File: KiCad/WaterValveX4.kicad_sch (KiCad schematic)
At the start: 51 parts, among them J1 Conn_01x04_Male, J2 Barrel_Jack, J3 Conn_01x03_Male, J4 Conn_01x01_Male, J5 Conn_01x04_Male, J6 Screw_Terminal_01x03, J7 Screw_Terminal_01x03, J8 Screw_Terminal_01x03, J9 Screw_Terminal_01x02, Q1 IRLML2502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

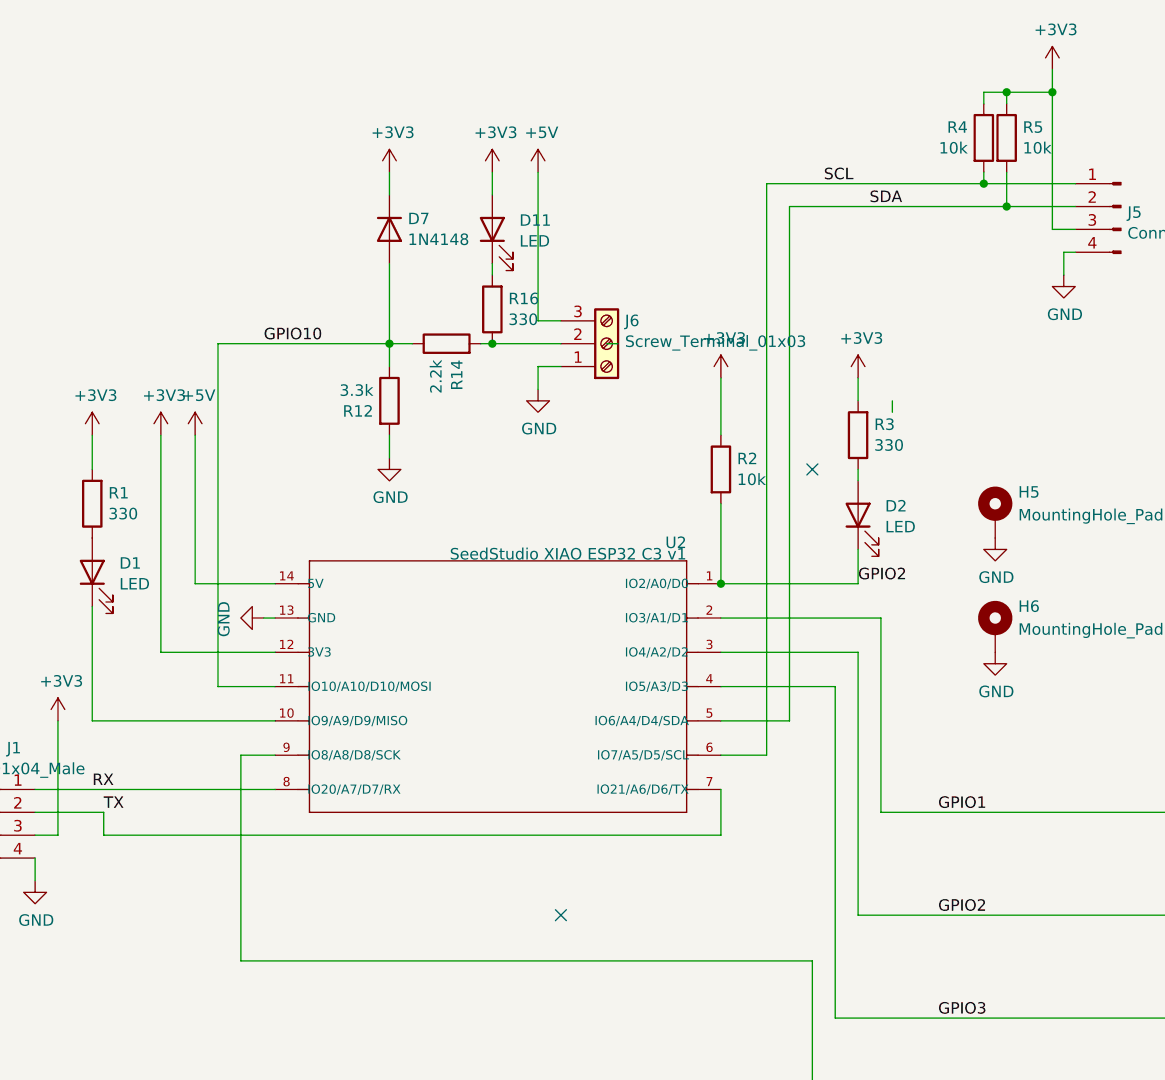
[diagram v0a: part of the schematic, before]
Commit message: Version 2.0.1 - pulled up / level shifted flow input
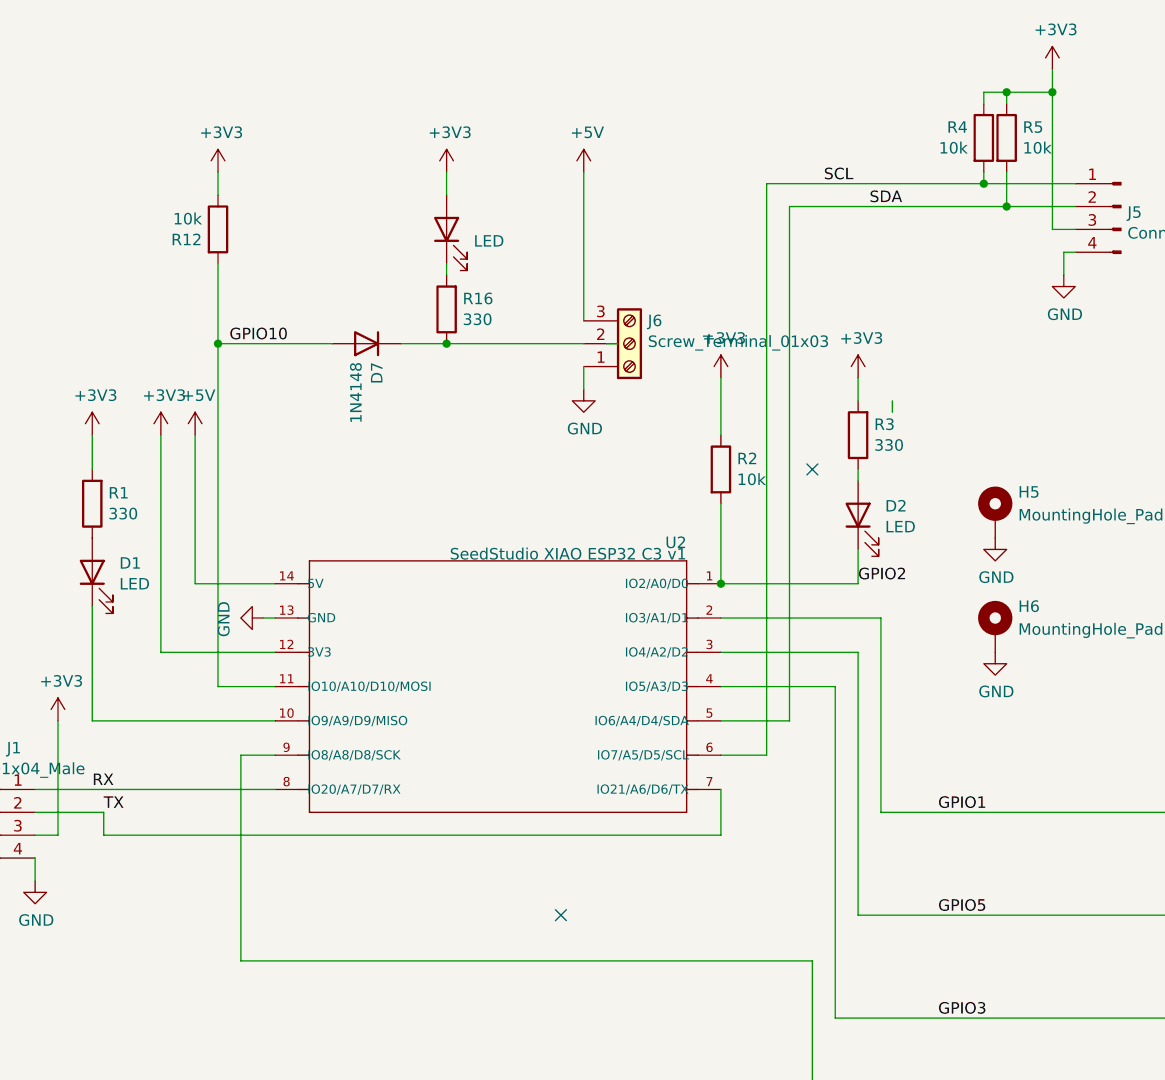
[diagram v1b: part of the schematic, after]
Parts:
- removed R14: 2.2k, Resistor_SMD:R_0805_2012Metric_Pad1.20x1.40mm_HandSolder, symbol Device:R
- R12: value 3.3k -> 10k
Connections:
- net +3V3: now also R12.1; no longer D7.1 (K)
- net GND: no longer R12.2
- net GPIO10: now also R12.2; no longer R12.1
- net GPIO2: no longer R8.1, U2.3 (IO4/A2/D2)
- net at J6.2 (Pin_2), R16.1: now also D7.1 (K)
- new net GPIO5: R8.1, U2.3 (IO4/A2/D2)
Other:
- moved on the sheet: J6, R16

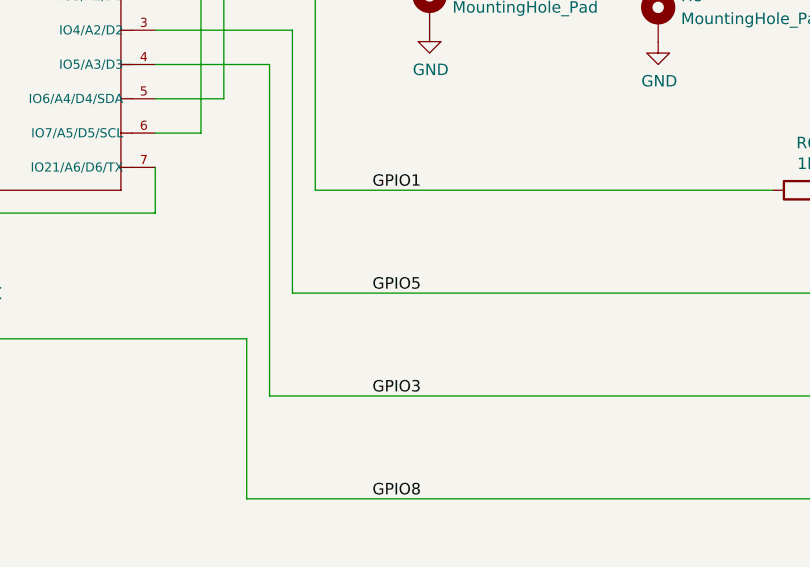
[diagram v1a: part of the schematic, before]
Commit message: Fixed KiCAD GPIO labels
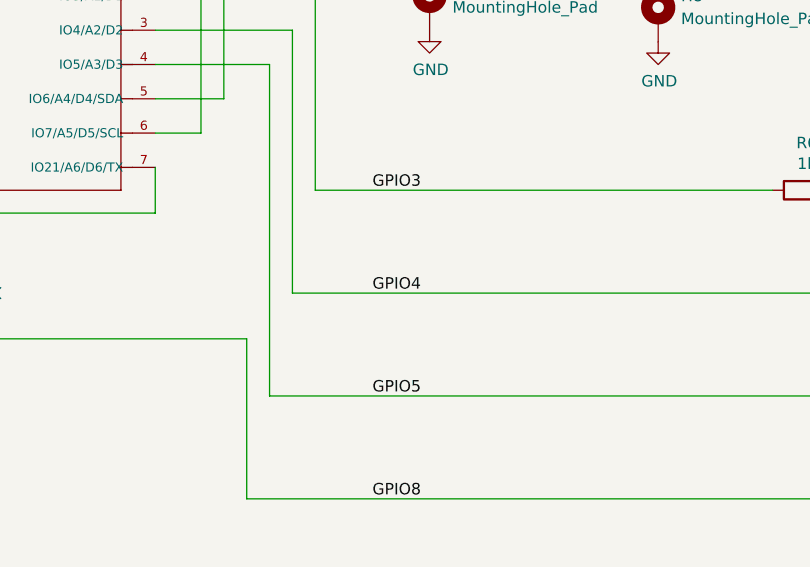
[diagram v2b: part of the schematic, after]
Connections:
- net GPIO1 is gone; now on net GPIO3: R6.1, U2.2 (IO3/A1/D1)
- net GPIO3: no longer R9.1, U2.4 (IO5/A3/D3)
- net GPIO5: now also R9.1, U2.4 (IO5/A3/D3); no longer R8.1, U2.3 (IO4/A2/D2)
- new net GPIO4: R8.1, U2.3 (IO4/A2/D2)
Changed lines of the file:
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@@
 		)
 	)
-	(label "GPIO5"
+	(label "GPIO4"
 		(at 125.73 115.57 0)
 		(fields_autoplaced yes)
@@
 		)
 	)
-	(label "GPIO3"
+	(label "GPIO5"
 		(at 125.73 127 0)
 		(fields_autoplaced yes)
@@
 		)
 	)
-	(label "GPIO1"
+	(label "GPIO3"
 		(at 125.73 104.14 0)
 		(fields_autoplaced yes)

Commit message: Change to use ESP32 C6 THT
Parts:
- removed U2: SeedStudio XIAO ESP32 C3 v1, LOCAL1:XIAO_ESP32C3_THT, symbol LOCAL1:XIAO_ESP32C3_THT
- added U2: XIAO-ESP32-C6, LOCAL1:XIAO-ESP32-C6-DIP, symbol LOCAL1:XIAO_ESP32-C6-DIP
- D11: footprint LED_SMD:LED_0805_2012Metric_Pad1.15x1.40mm_HandSolder -> LED_THT:LED_D5.0mm
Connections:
- net +3V3: now also U2.12 (3V3)
- net +5V: now also U2.14 (VBUS)
- net GND: now also U2.13 (GND)
- net GPIO10: now also U2.11 (GPIO18/D10/MOSI)
- net GPIO2: now also U2.1 (GPIO0/A0/D0)
- net GPIO3: now also U2.2 (GPIO1/A1/D1)
- net GPIO4: now also U2.3 (GPIO2/A2/D2)
- net GPIO5: now also U2.4 (GPIO21/D3)
- net GPIO8: now also U2.9 (GPIO19/D8/SCK)
- net RX: now also U2.8 (GPIO17/D7/RX)
- net SCL: now also U2.6 (GPIO23/D5/SCL)
- net SDA: now also U2.5 (GPIO22/D4/SDA)
- net TX: now also U2.7 (GPIO16/D6/TX)
- net at D1.1 (K): now also U2.10 (GPIO20/D9/MISO)
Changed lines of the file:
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@@
 (kicad_sch
-	(version 20231120)
+	(version 20250114)
 	(generator "eeschema")
-	(generator_version "8.0")
+	(generator_version "9.0")
 	(paper "A4")
 	(title_block
@@
 		(comment 2 "Project documents are licensed under CC-BY-SA 2.0")
 	)
+	(text "IO1  - Valve 1\nIO2  - Valve 2\nIO3  - Valve 3\nIO8  - Valve 4\nIO9  - LED\nIO10 - Water meter\n\n 2 - 8 - 9 \n -   -   H   normal\n 1   NA  1   SPI boot (default) Flash boot\n 1   1   0   Download\n\n"
+		(exclude_from_sim no)
+		(at 191.77 67.31 0)
+		(effects
+			(font
+				(size 2.54 2.54)
+			)
+			(justify left bottom)
+		)
+	)
 	(junction
 		(at 86.36 176.53)
@@
 	)
 	(junction
+		(at 101.6 78.74)
+		(diameter 0)
+		(color 0 0 0 0)
+	)
+	(junction
 		(at 203.2 101.6)
 		(diameter 0)
@@
 	)
 	(junction
-		(at 101.6 78.74)
-		(diameter 0)
-		(color 0 0 0 0)
-	)
-	(junction
 		(at 133.35 24.13)
 		(diameter 0)
@@
 		)
 	)
-	(text "IO1  - Valve 1\nIO2  - Valve 2\nIO3  - Valve 3\nIO8  - Valve 4\nIO9  - LED\nIO10 - Water meter\n\n 2 - 8 - 9 \n -   -   H   normal\n 1   NA  1   SPI boot (default) Flash boot\n 1   1   0   Download\n\n"
-		(exclude_from_sim no)
-		(at 191.77 67.31 0)
-		(effects
-			(font
-				(size 2.54 2.54)
-			)
-			(justify left bottom)
-		)
-	)
 	(label "GPIO4"
 		(at 125.73 115.57 0)
-		(fields_autoplaced yes)
 		(effects
 			(font
@@
 	(label "Relay1"
 		(at 218.44 107.95 0)
-		(fields_autoplaced yes)
 		(effects
 			(font
@@
 	(label "TX"
 		(at 33.02 104.14 0)
-		(fields_autoplaced yes)
 		(effects
 			(font
@@
 	(label "GPIO5"
 		(at 125.73 127 0)
-		(fields_autoplaced yes)
 		(effects
 			(font
@@
 	(label "GPIO10"
 		(at 46.99 52.07 0)
-		(fields_autoplaced yes)
 		(effects
 			(font
@@
 	(label "Relay3"
 		(at 218.44 101.6 0)
-		(fields_autoplaced yes)
 		(effects
 			(font
@@
 	(label "GPIO2"
 		(at 116.84 78.74 0)
-		(fields_autoplaced yes)
 		(effects
 			(font
@@
 	(label "SCL"
 		(at 113.03 34.29 0)
-		(fields_autoplaced yes)
 		(effects
 			(font
@@
 	(label "GPIO8"
 		(at 125.73 138.43 0)
-		(fields_autoplaced yes)
 		(effects
 			(font
@@
 	(label "GPIO3"
 		(at 125.73 104.14 0)
-		(fields_autoplaced yes)
 		(effects
 			(font
@@
 	(label "Relay2"
 		(at 218.44 105.41 0)
-		(fields_autoplaced yes)
 		(effects
 			(font
@@
 	(label "PwrIn"
 		(at 71.12 176.53 0)
-		(fields_autoplaced yes)
 		(effects
 			(font
@@
 	(label "SDA"
 		(at 118.11 36.83 0)
-		(fields_autoplaced yes)
 		(effects
 			(font
@@
 	(label "RX"
 		(at 31.75 101.6 0)
-		(fields_autoplaced yes)
 		(effects
 			(font
@@
 	(label "Relay4"
 		(at 218.44 99.06 0)
-		(fields_autoplaced yes)
 		(effects
 			(font
@@
 	)
 	(symbol
-		(lib_id "LOCAL1:XIAO_ESP32C3_THT")
-		(at 76.2 90.17 0)
-		(mirror y)
-		(unit 1)
-		(exclude_from_sim no)
-		(in_bom yes)
-		(on_board yes)
-		(dnp no)
-		(property "Reference" "U2"
-			(at 97.79 74.93 0)
-			(effects
-				(font
-					(size 1.27 1.27)
-				)
-				(justify left bottom)
-			)
-		)
-		(property "Value" "SeedStudio XIAO ESP32 C3 v1"
-			(at 97.79 76.2 0)
-			(effects
-				(font
-					(size 1.27 1.27)
-				)
-				(justify left bottom)
-			)
-		)
-		(property "Footprint" "LOCAL1:XIAO_ESP32C3_THT"
-			(at 76.2 90.17 0)
-			(effects
-				(font
-					(size 1.27 1.27)
-				)
-				(justify bottom)
-				(hide yes)
-			)
-		)
-		(property "Datasheet" "https://files.seeedstudio.com/wiki/XIAO_WiFi/Resources/esp32-c3_datasheet.pdf"
-			(at 76.2 90.17 0)
-			(effects
-				(font
-					(size 1.27 1.27)
-				)
-				(hide yes)
-			)
-		)
-		(property "Description" ""
-			(at 76.2 90.17 0)
-			(effects
-				(font
-					(size 1.27 1.27)
-				)
-				(hide yes)
-			)
-		)
-		(pin "1"
-		)
-		(pin "10"
-		)
-		(pin "11"
-		)
-		(pin "12"
-		)
-		(pin "13"
-		)
-		(pin "14"
-		)
-		(pin "2"
-		)
-		(pin "3"
-		)
-		(pin "4"
-		)
-		(pin "5"
-		)
-		(pin "6"
-		)
-		(pin "7"
-		)
-		(pin "8"
-		)
-		(pin "9"
-		)
-		(instances
-			(project "WaterX4"
-				(path "/098a8407-cb75-4379-a694-65a64d739020"
-					(reference "U2")
-					(unit 1)
-				)
-			)
-		)
-	)
-	(symbol
 		(lib_id "Device:R")
 		(at 173.99 104.14 90)
@@
 				)
 				(justify right)
-				(hide yes)
 			)
 		)
@@
 			)
 		)
-		(property "Footprint" "LED_SMD:LED_0805_2012Metric_Pad1.15x1.40mm_HandSolder"
+		(property "Footprint" "LED_THT:LED_D5.0mm"
 			(at 71.12 39.37 0)
 			(effects
@@
 		)
 	)
+	(symbol
+		(lib_id "LOCAL1:XIAO_ESP32-C6-DIP")
+		(at 77.47 90.17 0)
+		(mirror y)
+		(unit 1)
+		(exclude_from_sim no)
+		(in_bom yes)
+		(on_board yes)
+		(dnp no)
+		(property "Reference" "U2"
+			(at 76.835 71.12 0)
+			(effects
+				(font
+					(size 1.27 1.0795)
+				)
+			)
+		)
+		(property "Value" "XIAO-ESP32-C6"
+			(at 76.835 73.66 0)
+			(effects
+				(font
+					(size 1.27 1.0795)
+				)
+			)
+		)
+		(property "Footprint" "LOCAL1:XIAO-ESP32-C6-DIP"
+			(at 82.042 108.712 0)
+			(effects
+				(font
+					(size 1.27 1.27)
+				)
+				(hide yes)
+			)
+		)
+		(property "Datasheet" ""
+			(at 77.47 90.17 0)
+			(effects
+				(font
+					(size 1.27 1.27)
+				)
+				(hide yes)
+			)
+		)
+		(property "Description" ""
+			(at 77.47 90.17 0)
+			(effects
+				(font
+					(size 1.27 1.27)
+				)
+				(hide yes)
+			)
+		)
+		(property "Manufacturer" ""
+			(at 77.47 90.17 0)
+			(effects
+				(font
+					(size 1.27 1.27)
+				)
+				(hide yes)
+			)
+		)
+		(property "MPN" ""
+			(at 77.47 90.17 0)
+			(effects
+				(font
+					(size 1.27 1.27)
+				)
+				(hide yes)
+			)
+		)
+		(property "SKU" "XIAO-DIP"
+			(at 83.312 92.456 0)
+			(effects
+				(font
+					(size 1.27 1.27)
+				)
+				(hide yes)
+			)
+		)
+		(property "Part Type" ""
+			(at 77.47 90.17 0)
+			(effects
+				(font
+					(size 1.27 1.27)
+				)
+				(hide yes)
+			)
+		)
+		(property "Rating" ""
+			(at 77.47 90.17 0)
+			(effects
+				(font
+					(size 1.27 1.27)
+				)
+			)
+		)
+		(property "Status" ""
+			(at 77.47 90.17 0)
+			(effects
+				(font
+					(size 1.27 1.27)
+				)
+				(hide yes)
+			)
+		)
+		(property "Temperature" ""
+			(at 77.47 90.17 0)
+			(effects
+				(font
+					(size 1.27 1.27)
+				)
+				(hide yes)
+			)
+		)
+		(property "Priority" ""
+			(at 77.47 90.17 0)
+			(effects
+				(font
+					(size 1.27 1.27)
+				)
+				(hide yes)
+			)
+		)
+		(pin "11"
+		)
+		(pin "12"
+		)
+		(pin "10"
+		)
+		(pin "9"
+		)
+		(pin "8"
+		)
+		(pin "5"
+		)
+		(pin "3"
+		)
+		(pin "6"
+		)
+		(pin "7"
+		)
+		(pin "4"
+		)
+		(pin "14"
+		)
+		(pin "2"
+		)
+		(pin "1"
+		)
+		(pin "13"
+		)
+		(instances
+			(project ""
+				(path "/098a8407-cb75-4379-a694-65a64d739020"
+					(reference "U2")
+					(unit 1)
+				)
+			)
+		)
+	)
 	(sheet_instances
 		(path "/"
@@
 		)
 	)
+	(embedded_fonts no)
 )

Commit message: Optimized layout - passes most DRC checks
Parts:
- added D13: LED, LED_SMD:LED_0805_2012Metric_Pad1.15x1.40mm_HandSolder, symbol Device:LED
- added D14, D15, D16, D17, D18: LED, LED_THT:LED_D3.0mm, symbol Device:LED
- D11: footprint LED_THT:LED_D5.0mm -> LED_THT:LED_D3.0mm
- D12, D4, D6, D9: footprint Diode_THT:D_DO-41_SOD81_P3.81mm_Vertical_KathodeUp -> Diode_THT:D_DO-41_SOD81_P2.54mm_Vertical_KathodeUp
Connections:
- net +3V3: now also D13.2 (A), D14.2 (A)
- net +VSW: now also D15.2 (A), D16.2 (A), D17.2 (A), D18.2 (A)
- net at D3.1 (K), R7.2: now also D15.1 (K)
- net at D5.1 (K), R10.2: now also D16.1 (K)
- net at D8.1 (K), R13.2: now also D17.1 (K)
- net at D10.1 (K), R15.2: now also D18.1 (K)
- net at D11.1 (K), R16.2: now also D13.1 (K)
- net at D1.2 (A), R1.1: now also D14.1 (K)
- net GPIO10 renamed D10
- net GPIO3 renamed D1
- net GPIO4 renamed D2
- net GPIO5 renamed D3
- net GPIO8 renamed D8
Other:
- note added: "D1 - Valve 1 D2 - Valve 2 D3 - Valve 3 D8 - Valve 4 D9 - LED D10 - Water meter 2 - 8 - 9 - - H normal 1 NA 1 SPI boot (default) Flash boot 1 1 0 Download"
- note removed: "IO1 - Valve 1 IO2 - Valve 2 IO3 - Valve 3 IO8 - Valve 4 IO9 - LED IO10 - Water meter 2 - 8 - 9 - - H normal 1 NA 1 SPI boot (default) Flash boot 1 1 0 Download"
- moved on the sheet: D10, D12, D3, D4, D5, D6, D8, D9, H7, H8, Q1, Q2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
